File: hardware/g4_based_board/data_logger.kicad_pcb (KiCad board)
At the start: 4 copper layers, 290 parts, among them J1 Conn_01x07_Socket, J10 Screw_Terminal_01x03, J11 Screw_Terminal_01x03, J12 Conn_02x03_Odd_Even, J13 Conn_02x03_Odd_Even, J14 DE9_Receptacle, J15 Screw_Terminal_01x03, J16 Screw_Terminal_01x03, J17 Screw_Terminal_01x03, J18 Screw_Terminal_01x03, J19 Screw_Terminal_01x03, J2 Conn_02x07_Odd_Even, J20 Screw_Terminal_01x03, J21 Screw_Terminal_01x03, J22 Screw_Terminal_01x03, J23 Screw_Terminal_01x03, J24 Screw_Terminal_01x03, J25 Screw_Terminal_01x03, J26 Conn_02x03_Odd_Even, J27 Conn_02x03_Odd_Even, J28 DE9_Receptacle, J29 Screw_Terminal_01x03, J3 Conn_01x07_Socket, J30 Conn_02x03_Odd_Even, J31 Conn_02x03_Odd_Even, J32 DE9_Receptacle, J33 Conn_02x03_Odd_Even, J34 Conn_02x03_Odd_Even, J35 DE9_Receptacle, J36 Conn_02x03_Odd_Even, J37 Conn_02x03_Odd_Even, J38 DE9_Receptacle, J4 Conn_02x03_Odd_Even, J5 Conn_02x03_Odd_Even, J6 DE9_Receptacle, J7 Conn_01x05_Socket, J8 USB_C_Receptacle_USB2.0, J9 Micro_SD_Card_Det1, Q1 NPN, Q10 NMOS, Q11 NMOS, Q12 NMOS, Q13 NMOS, Q14 NMOS, Q15 NMOS, Q16 NMOS, Q17 NMOS, Q2 NPN, Q3 NMOS, Q4 NMOS, Q5 BC547, Q6 NMOS, Q7 NMOS, Q8 NMOS, Q9 NMOS, SW1 RESET, SW2 SW_SPDT, U1 STM32G431R6Tx, U2 MCP9804_MSOP, U3 MCP3428x-xST, U4 TXS0102DCT, U5 PCF8574, U6 tps2117, U7 AZ1117-3.3

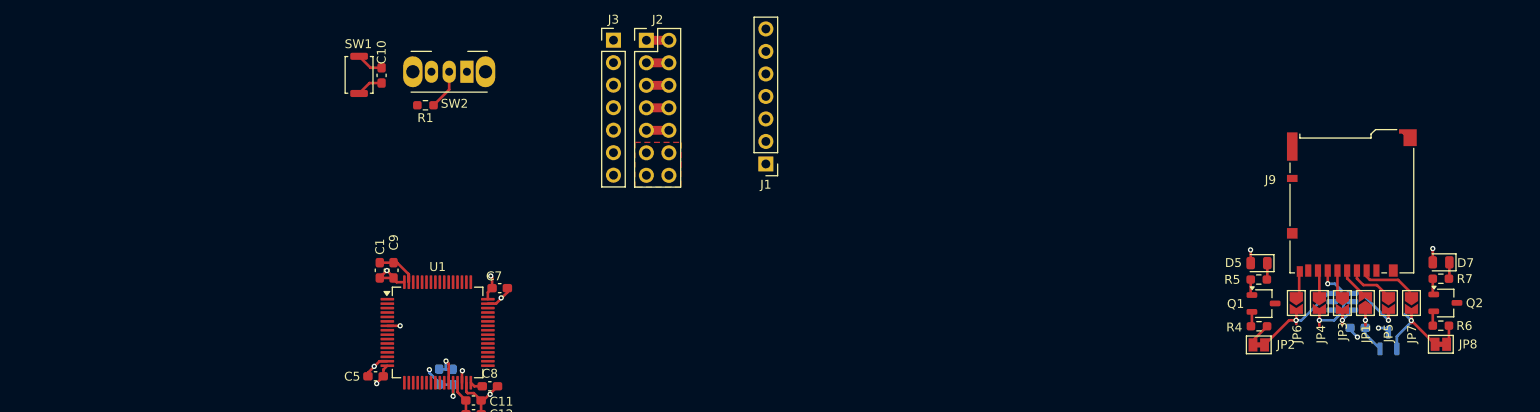
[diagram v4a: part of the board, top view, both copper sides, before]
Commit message: added buttons
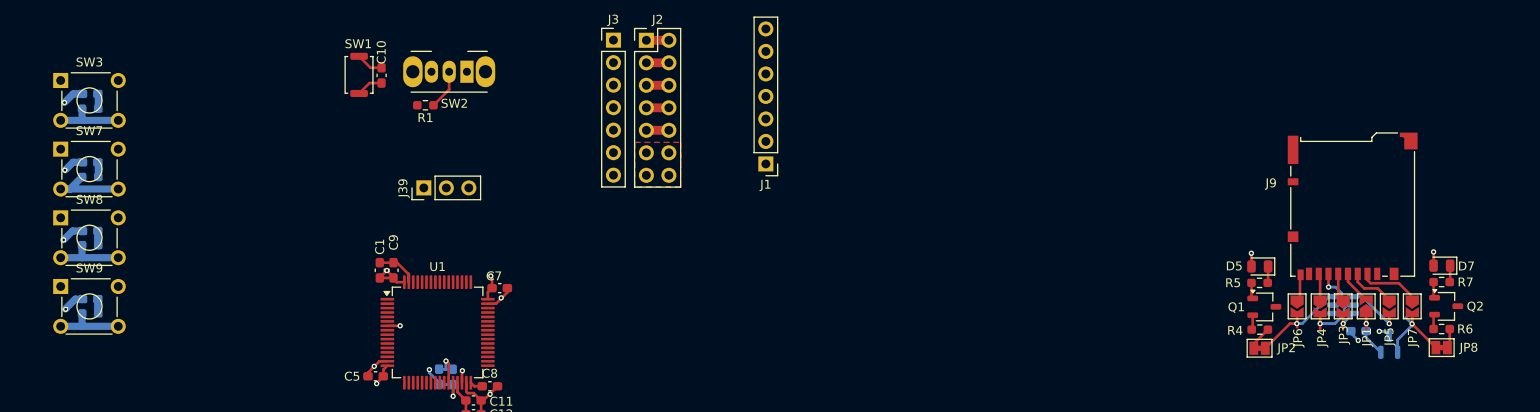
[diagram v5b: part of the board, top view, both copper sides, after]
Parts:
- added C53: C, Capacitor_SMD:C_0603_1608Metric_Pad1.08x0.95mm_HandSolder, B.Cu at (60.5, 26.6)
- added C54: C, Capacitor_SMD:C_0603_1608Metric_Pad1.08x0.95mm_HandSolder, B.Cu at (60.5, 34.3)
- added C55: C, Capacitor_SMD:C_0603_1608Metric_Pad1.08x0.95mm_HandSolder, B.Cu at (60.5, 42.1)
- added C56: C, Capacitor_SMD:C_0603_1608Metric_Pad1.08x0.95mm_HandSolder, B.Cu at (60.5, 49.8)
- added J39: Conn_01x03, Connector_PinHeader_2.54mm:PinHeader_1x03_P2.54mm_Vertical, F.Cu at (98.2, 37.2)
- added R73: R, Resistor_SMD:R_0603_1608Metric_Pad0.98x0.95mm_HandSolder, B.Cu at (60.5, 28.3)
- added R75: R, Resistor_SMD:R_0603_1608Metric_Pad0.98x0.95mm_HandSolder, B.Cu at (60.5, 36.0)
- added R77: R, Resistor_SMD:R_0603_1608Metric_Pad0.98x0.95mm_HandSolder, B.Cu at (60.5, 43.7)
- added R79: R, Resistor_SMD:R_0603_1608Metric_Pad0.98x0.95mm_HandSolder, B.Cu at (60.5, 51.4)
- added SW3: DOWN, Button_Switch_THT:SW_TH_Tactile_Omron_B3F-10xx, F.Cu at (57.2, 25.1)
- added SW7: DOWN, Button_Switch_THT:SW_TH_Tactile_Omron_B3F-10xx, F.Cu at (57.2, 32.9)
- added SW8: DOWN, Button_Switch_THT:SW_TH_Tactile_Omron_B3F-10xx, F.Cu at (57.2, 40.6)
- added SW9: DOWN, Button_Switch_THT:SW_TH_Tactile_Omron_B3F-10xx, F.Cu at (57.2, 48.4)
- moved D4 0.39 mm to (201.9, 50.4)
- moved R7 0.39 mm to (213.1, 47.9)
- moved JP2 0.39 mm to (192.5, 55.3)
- moved Q2 0.39 mm to (213.6, 50.6)
- moved R5 0.39 mm to (192.5, 47.9)
- moved C13 0.39 mm to (203.7, 53.4)
- moved D5 0.39 mm to (192.5, 46.1)
- moved D6 0.39 mm to (207.2, 54.8)
- moved D7 0.39 mm to (213.1, 46.0)
- moved J9 0.39 mm to (203.0, 39.3)
- moved JP1 0.39 mm to (204.6, 50.6)
- moved JP4 0.39 mm to (199.3, 50.6)
- moved JP5 0.39 mm to (207.2, 50.6)
- moved JP6 0.39 mm to (196.8, 50.6)
- moved JP7 0.39 mm to (209.8, 50.6)
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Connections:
- U1 pad 17: unconnected-(U1-PA3-Pad17) -> /analog_digital_io/GPIO-4
- U1 pad 22: /analog_digital_io/GPIO-11 -> /interface/SD_CONNECTED
- U1 pad 24: unconnected-(U1-PB0-Pad24) -> /analog_digital_io/GPIO-11
- U1 pad 26: unconnected-(U1-PB2-Pad26) -> /interface/WAKE_BTN
- U1 pad 30: unconnected-(U1-PB10-Pad30) -> /interface/ENTER_BTN
- U1 pad 33: unconnected-(U1-PB11-Pad33) -> /interface/DOWN_BTN
- U1 pad 34: /interface/SD_CONNECTED -> /analog_digital_io/GPIO-3
- U1 pad 35: /interface/SCLK -> /high_speed_digital/EN_1
- U1 pad 36: /interface/MISO -> /high_speed_digital/EN_2
- U1 pad 37: /interface/MOSI -> /high_speed_digital/EN_3
- U1 pad 42: /analog_digital_io/GPIO-3 -> unconnected-(U1-PA8-Pad42)
- U1 pad 50: /high_speed_digital/SDA -> /mcu/USART_TX
- U1 pad 51: /analog_digital_io/GPIO-4 -> /mcu/USART_RX
- U1 pad 52: /high_speed_digital/EN_1 -> /interface/SCLK
- U1 pad 53: /high_speed_digital/EN_2 -> /interface/MISO
- U1 pad 54: /high_speed_digital/EN_3 -> /interface/MOSI
- U1 pad 58: unconnected-(U1-PB5-Pad58) -> /mcu/USART_CK
- U1 pad 60: unconnected-(U1-PB7-Pad60) -> /high_speed_digital/SDA
- U1 pad 62: unconnected-(U1-PB9-Pad62) -> /interface/UP_BTN
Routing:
- net GND: track 812.8 -> 822.4 mm, vias 64 -> 68
- net Net-(R75-Pad1): track 0.00 -> 9.48 mm
- net Net-(R79-Pad1): track 0.00 -> 7.97 mm
- net Net-(R77-Pad1): track 0.00 -> 7.92 mm
- net Net-(R73-Pad1): track 0.00 -> 7.86 mm
- net /interface/ENTER_BTN: track 0.00 -> 3.01 mm, vias 0 -> 1
- net /interface/DOWN_BTN: track 0.00 -> 1.70 mm
- net /interface/UP_BTN: track 0.00 -> 1.68 mm
- net /interface/WAKE_BTN: track 0.00 -> 1.63 mm
- net unconnected-(U1-PB10-Pad30): track 1.39 -> 0.00 mm, vias 1 -> 0

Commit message: rev-1
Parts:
- removed C14, C15, C16, C17, C26, C27, C28, C29, C30, C31, C32, C33, C34, C35, C36, C37, C38, C39, C40, C41, C42, C43, C44, C45, C46, C47, C48, C49: C, Capacitor_SMD:C_0603_1608Metric_Pad1.08x0.95mm_HandSolder
- removed C23, C24, C25: 100n, Capacitor_SMD:C_0603_1608Metric_Pad1.08x0.95mm_HandSolder
- removed D10, D11, D12, D13, D14, D15, D16, D17, D18, D19, D20, D21, D8, D9: SP0502BAHT, Package_TO_SOT_SMD:SOT-23
- removed DS1: WC1602A, Display:WC1602A
- removed H2, H4, H5, H6, H7, H9: MountingHole, MountingHole:MountingHole_3.2mm_M3
- removed J10, J11, J15, J16, J17, J18, J19, J20, J21, J22, J23, J24, J25, J29: Screw_Terminal_01x03, TerminalBlock:TerminalBlock_Altech_AK300-3_P5.00mm
- removed J14, J28, J32, J35, J38, J6: DE9_Receptacle, Connector_Dsub:DSUB-9_Female_Vertical_P2.77x2.84mm_MountingHoles
- removed J26, J27, J30, J31, J33, J34, J36, J37: Conn_02x03_Odd_Even, Connector_PinHeader_2.54mm:PinHeader_2x03_P2.54mm_Vertical
- removed JP10, JP13, JP26, JP29, JP32, JP35, JP38, JP41, JP44, JP47, JP50, JP53, JP56, JP59: pulldown, Connector_PinHeader_2.54mm:PinHeader_1x02_P2.54mm_Vertical
- removed JP11, JP14, JP27, JP30, JP33, JP36, JP39, JP42, JP45, JP48, JP51, JP54, JP57, JP60: power_select, Connector_PinHeader_2.54mm:PinHeader_1x03_P2.54mm_Vertical
- removed JP12, JP25, JP28, JP31, JP34, JP37, JP40, JP43, JP46, JP49, JP52, JP55, JP58, JP9: I/O select, Connector_PinHeader_2.54mm:PinHeader_1x03_P2.54mm_Vertical
- removed JP20, JP21, JP22: SolderJumper_3_Open, Jumper:SolderJumper-3_P1.3mm_Open_RoundedPad1.0x1.5mm
- removed JP23, JP24, JP5, JP6, JP7: Jumper_2_Open, Jumper:SolderJumper-2_P1.3mm_Open_TrianglePad1.0x1.5mm
- removed Q10, Q11, Q12, Q13, Q14, Q15, Q16, Q17, Q3, Q4, Q6, Q7, Q8, Q9: NMOS, Package_TO_SOT_SMD:SOT-23-3
- removed R10, R11, R12, R13, R14, R15, R22, R23, R24, R25, R26, R27, R28, R29, R30, R31, R32, R33, R34, R35, R36, R37, R38, R39, R40, R41, R42, R43, R44, R45, R46, R47, R48, R49, R50, R51, R52, R53, R54, R55, R56, R57, R58, R59, R60, R61, R62, R63, R64, R65, R66, R67, R68, R69, R8, R9: R, Resistor_SMD:R_0603_1608Metric_Pad0.98x0.95mm_HandSolder
- removed TP5: LCD_PWR, TestPoint:TestPoint_Pad_D1.5mm
- removed U5: PCF8574, Package_SO:SOIC-16W_7.5x10.3mm_P1.27mm
- added G***: LOGO, frogs:UC_LOGO, B.Cu at (188.0, 136.0)
- added G***: LOGO, frogs:frog_smol, B.Cu at (167.0, 105.0)
- added J40: Conn_01x07_Socket, Connector_PinHeader_2.54mm:PinHeader_1x07_P2.54mm_Vertical, F.Cu at (106.8, 141.1)
- added J43: Conn_01x06, Connector_PinHeader_2.54mm:PinHeader_1x06_P2.54mm_Vertical, B.Cu at (165.2, 78.1)
- added R74: 1k, Resistor_SMD:R_0603_1608Metric_Pad0.98x0.95mm_HandSolder, B.Cu at (141.6, 90.6)
- added R76: 1k, Resistor_SMD:R_0603_1608Metric_Pad0.98x0.95mm_HandSolder, B.Cu at (126.1, 90.6)
- added R78: 1k, Resistor_SMD:R_0603_1608Metric_Pad0.98x0.95mm_HandSolder, B.Cu at (133.8, 90.6)
- added RV2: 10k, Potentiometer_THT:Potentiometer_Vishay_T73YP_Vertical, B.Cu at (142.6, 65.2)
- added RV3: 10k, Potentiometer_THT:Potentiometer_Vishay_T73YP_Vertical, B.Cu at (134.7, 65.2)
- added RV4: 10k, Potentiometer_THT:Potentiometer_Vishay_T73YP_Vertical, B.Cu at (142.5, 88.6)
- added RV5: 10k, Potentiometer_THT:Potentiometer_Vishay_T73YP_Vertical, B.Cu at (126.9, 65.2)
- added RV6: 10k, Potentiometer_THT:Potentiometer_Vishay_T73YP_Vertical, B.Cu at (119.1, 65.2)
- added RV7: 10k, Potentiometer_THT:Potentiometer_Vishay_T73YP_Vertical, B.Cu at (127.1, 88.6)
- added RV8: 10k, Potentiometer_THT:Potentiometer_Vishay_T73YP_Vertical, B.Cu at (134.7, 88.6)
- C1, C11, C12, C5, C7, C8, C9, J2, J7, J9, JP1, JP15, JP16, JP17, R1, SW2, TC1, TC2, TC3, TC4, U1: moved to B.Cu
- C18, C19, C2, C20, C6, D4, D6, JP18, JP19, R16, U2, U3: moved to F.Cu
- C21, C22: value 100n -> C; moved to F.Cu
- J12: value Conn_02x03_Odd_Even -> Screw_Terminal_01x04; footprint Connector_PinHeader_2.54mm:PinHeader_2x03_P2.54mm_Vertical -> TerminalBlock:TerminalBlock_Altech_AK300-4_P5.00mm; moved to B.Cu
- J13: value Conn_02x03_Odd_Even -> Conn_01x09_Pin; footprint Connector_PinHeader_2.54mm:PinHeader_2x03_P2.54mm_Vertical -> Connector_PinHeader_2.54mm:PinHeader_1x09_P2.54mm_Vertical; moved to B.Cu
- J4: value Conn_02x03_Odd_Even -> Conn_01x04; footprint Connector_PinHeader_2.54mm:PinHeader_2x03_P2.54mm_Vertical -> Connector_Molex:Molex_KK-254_AE-6410-04A_1x04_P2.54mm_Vertical
- J5: value Conn_02x03_Odd_Even -> Screw_Terminal_01x03; footprint Connector_PinHeader_2.54mm:PinHeader_2x03_P2.54mm_Vertical -> TerminalBlock:TerminalBlock_Altech_AK300-3_P5.00mm; moved to B.Cu
- JP3: value Jumper_2_Open -> power_select; footprint Jumper:SolderJumper-2_P1.3mm_Open_TrianglePad1.0x1.5mm -> Connector_PinHeader_2.54mm:PinHeader_1x03_P2.54mm_Vertical; moved to B.Cu
- JP4: value Jumper_2_Open -> Jumper_3_Bridged12; footprint Jumper:SolderJumper-2_P1.3mm_Open_TrianglePad1.0x1.5mm -> Connector_PinHeader_2.54mm:PinHeader_1x03_P2.54mm_Vertical; moved to B.Cu
- Q5: value BC547 -> NMOS
- R17, R18: value R -> 0; moved to F.Cu
- R19, R20: value 10k -> R
- R21: value 120 -> 1k
- RV1: footprint Potentiometer_THT:Potentiometer_Vishay_T73XX_Horizontal -> Potentiometer_THT:Potentiometer_Vishay_T73YP_Vertical
- SW7: value DOWN -> UP
- SW8: value DOWN -> ENTER
- SW9: value DOWN -> WAKE
- U4: value TXS0102DCT -> TL074; footprint Package_SO:SSOP-8_2.95x2.8mm_P0.65mm -> Package_SO:SOIC-14_3.9x8.7mm_P1.27mm
- moved H10 195.4 mm to (199.6, 146.8)
- moved H8 173.1 mm to (199.4, 54.2)
- moved R1 135.4 mm to (197.1, 120.6), turned to 90 degrees
- moved SW2 134.1 mm to (200.8, 115.9), turned to -90 degrees
- moved SW1 133.3 mm to (200.1, 100.9), turned to 180 degrees
- moved C10 130.7 mm to (197.6, 103.5), turned to 0 degrees
- moved C18 130.4 mm to (135.2, 145.7)
- moved R16 129.3 mm to (135.2, 144.2)
- moved TC3 129.2 mm to (149.5, 144.0)
- moved TC2 129.2 mm to (115.8, 144.0)
- moved TC4 129.2 mm to (138.3, 144.0)
- moved TC1 129.2 mm to (127.0, 144.0)
- moved R21 128.4 mm to (118.3, 90.7)
- moved R17 128.1 mm to (135.2, 142.6)
- moved J13 127.8 mm to (150.8, 77.7), turned to 180 degrees
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- renumbered TP31 to 3.3V, TP30 to 5v, TP32 to GND
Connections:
- C21 pad 1: /high_speed_digital/LCD1/LCD_Power_3.3 -> Net-(J5-Pin_1)
- C22 pad 1: /high_speed_digital/LCD1/LCD_Power -> Net-(JP4-C)
- D4 pad 3: /interface/SD_CONNECTED -> /interface/MOSI
- D4 pad 4: /interface/MOSI -> /interface/SCLK
- D4 pad 6: /interface/SCLK -> /interface/SD_CONNECTED
- D6 pad 1: /interface/SD_SELECT -> Net-(J5-Pin_1)
- D6 pad 2: +3.3V -> Net-(J5-Pin_2)
- J12 pad 1: +3.3V -> /analog_in/SIG_IN_1
- J12 pad 2: Net-(J12-Pin_2) -> /analog_in/SIG_IN_2
- J12 pad 3: +VDC -> /analog_in/SIG_IN_3
- J12 pad 4: Net-(J12-Pin_2) -> /analog_in/SIG_IN_4
- J13 pad 1: +BATT -> /mcu/ADC-GPIO-PWM-12
- J13 pad 2: Net-(J13-Pin_2) -> /mcu/DAC2_OUT-ADC-GPIO-PWM
- J13 pad 3: -VDC -> /mcu/DAC1_OUT-ADC-GPIO-PWM
- J13 pad 4: Net-(J13-Pin_2) -> /mcu/ADC-GPIO-PWM-4
- J13 pad 5: +5V -> /mcu/ADC-GPIO-PWM-2-DIFF1-2
- J13 pad 6: Net-(J13-Pin_2) -> /mcu/ADC-GPIO-PWM-1-DIFF1-1
- J2 pad 1: +5V -> +3.3V
- J2 pad 10: -VDC -> +BATT
- J2 pad 2: +5V -> +3.3V
- J2 pad 3: +3.3V -> +5V
- J2 pad 4: +3.3V -> +5V
- J2 pad 5: +BATT -> -VDC
- J2 pad 6: +BATT -> -VDC
- J2 pad 9: -VDC -> +BATT
- J39 pad 2: /mcu/USART_RX -> /mcu/USART_TX
- J39 pad 3: /mcu/USART_TX -> /mcu/USART_RX
- J4 pad 1: +3.3V -> /high_speed_digital/I2C_CLK
- J4 pad 2: Net-(J4-Pin_2) -> /high_speed_digital/SDA
- J4 pad 3: +VDC -> +3.3V
- J4 pad 4: Net-(J4-Pin_2) -> GND
- J5 pad 1: +BATT -> Net-(J5-Pin_1)
- J5 pad 3: -VDC -> GND
- J7 pad 3: /high_speed_digital/SCLK -> /high_speed_digital/MISO
- J7 pad 5: /high_speed_digital/MISO -> /high_speed_digital/SCLK
- JP3 pad 1: /interface/SCLK -> +5V
- JP3 pad 2: /interface/SCLK -> Net-(J5-Pin_1)
- JP4 pad 1: /interface/MISO -> +5V
- JP4 pad 2: /interface/MISO -> Net-(JP4-C)
- Q5 pad 1: Net-(DS1-LED(-)) -> Net-(J5-Pin_2)
- Q5 pad 2: Net-(Q5-B) -> Net-(Q5-G)
- Q5 pad 3: GND -> Net-(Q5-S)
- R19 pad 1: Net-(U4-OE) -> Net-(Q5-G)
- R19 pad 2: GND -> /mcu/ADC-GPIO-PWM-11
- R20 pad 1: Net-(Q5-B) -> Net-(Q5-S)
- R20 pad 2: /high_speed_digital/LCD1/led -> GND
- R21 pad 1: /high_speed_digital/LCD1/LCD_Power -> GND
- R21 pad 2: Net-(DS1-LED(+)) -> Net-(U4B--)
- RV1 pad 1: GND -> Net-(U4B--)
- RV1 pad 2: Net-(DS1-VO) -> /mcu/HSE_IN
- RV1 pad 3: /high_speed_digital/LCD1/LCD_Power -> GND
- U1 pad 10: /analog_digital_io/GPIO-9 -> /mcu/ADC-GPIO-PWM-9
- U1 pad 11: /analog_digital_io/GPIO-10 -> /mcu/ADC-GPIO-PWM-10
- U1 pad 12: /analog_digital_io/GPIO-1 -> /mcu/ADC-GPIO-PWM-1-DIFF1-1
- U1 pad 13: /analog_digital_io/GPIO-2 -> /mcu/ADC-GPIO-PWM-2-DIFF1-2
- U1 pad 14: unconnected-(U1-PA2-Pad14) -> /interface/WAKE_BTN
- U1 pad 17: /analog_digital_io/GPIO-4 -> /mcu/ADC-GPIO-PWM-4
- U1 pad 18: /analog_digital_io/GPIO-2-DAC -> /mcu/DAC1_OUT-ADC-GPIO-PWM
- U1 pad 19: /analog_digital_io/GPIO-1-DAC -> /mcu/DAC2_OUT-ADC-GPIO-PWM
- U1 pad 2: /high_speed_digital/EN_4 -> /interface/DOWN_BTN
- U1 pad 22: /interface/SD_CONNECTED -> unconnected-(U1-PC4-Pad22)
- U1 pad 23: /analog_digital_io/GPIO-12 -> /mcu/ADC-GPIO-PWM-12
- U1 pad 24: /analog_digital_io/GPIO-11 -> /mcu/ADC-GPIO-PWM-11
- U1 pad 25: unconnected-(U1-PB1-Pad25) -> /mcu/DIGITAL_IO_EN_4
- U1 pad 26: /interface/WAKE_BTN -> /mcu/PWR_STATUS
- U1 pad 3: /high_speed_digital/EN_5 -> /interface/UP_BTN
- U1 pad 30: /interface/ENTER_BTN -> /mcu/DIGITAL_IO_EN_5
- U1 pad 33: /interface/DOWN_BTN -> /mcu/DIGITAL_IO_EN_6
- U1 pad 34: /analog_digital_io/GPIO-3 -> /mcu/ADC-GPIO-PWM-3
- U1 pad 35: /high_speed_digital/EN_1 -> /mcu/DIGITAL_IO_EN_1
- U1 pad 36: /high_speed_digital/EN_2 -> /mcu/DIGITAL_IO_EN_2
- U1 pad 37: /high_speed_digital/EN_3 -> /mcu/DIGITAL_IO_EN_3
- U1 pad 38: /interface/SD_SELECT -> /mcu/COMMS_EN_1
- U1 pad 39: /mcu/COMMS_EN_1 -> /mcu/COMMS_EN_2
- U1 pad 4: /high_speed_digital/EN_6 -> /interface/ENTER_BTN
- U1 pad 40: /mcu/COMMS_EN_2 -> /mcu/COMMS_EN_3
- U1 pad 41: /mcu/COMMS_EN_3 -> /interface/SD_SELECT
- U1 pad 55: /mcu/PWR_STATUS -> unconnected-(U1-PD2-Pad55)
- U1 pad 62: /interface/UP_BTN -> /interface/SD_CONNECTED
- U1 pad 8: /analog_digital_io/GPIO-7 -> /analog_in/ADC_4
- U1 pad 9: /analog_digital_io/GPIO-8 -> /analog_in/ADC_2
- U4 pad 1: /high_speed_digital/LCD1/5v_SDA -> /analog_in/ADC_2
- U4 pad 2: GND -> Net-(U4A--)
- U4 pad 3: /high_speed_digital/LCD1/LCD_Power_3.3 -> Net-(U4A-+)
- U4 pad 4: /high_speed_digital/SDA -> Net-(JP4-C)
- U4 pad 5: /high_speed_digital/I2C_CLK -> Net-(U4B-+)
- U4 pad 6: Net-(U4-OE) -> Net-(U4B--)
- U4 pad 7: /high_speed_digital/LCD1/LCD_Power -> /mcu/HSE_IN
- U4 pad 8: /high_speed_digital/LCD1/5v_SCL -> /mcu/HSE_OUT
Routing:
- net GND: track 822.4 -> 108.1 mm, vias 68 -> 46
- net +5V: track 32.8 -> 212.1 mm, vias 4 -> 2
- net -VDC: track 2.54 -> 170.1 mm, vias 0 -> 2
- net +BATT: track 2.54 -> 168.9 mm, vias 0 -> 2
- net +VDC: track 2.54 -> 166.6 mm, vias 0 -> 2
- net +3.3V: track 50.7 -> 177.1 mm, vias 16 -> 17
- net Net-(J21-Pin_2): track 103.2 -> 0.00 mm, vias 3 -> 0
- net Net-(J22-Pin_2): track 103.2 -> 0.00 mm, vias 3 -> 0
- net Net-(J16-Pin_2): track 103.2 -> 0.00 mm, vias 3 -> 0
- net Net-(J10-Pin_2): track 103.2 -> 0.00 mm, vias 3 -> 0
- net Net-(J23-Pin_2): track 103.2 -> 0.00 mm, vias 3 -> 0
- net Net-(J24-Pin_2): track 103.2 -> 0.00 mm, vias 3 -> 0
- net Net-(J20-Pin_2): track 103.2 -> 0.00 mm, vias 3 -> 0
- net Net-(J18-Pin_2): track 103.2 -> 0.00 mm, vias 3 -> 0
- net Net-(J15-Pin_2): track 103.2 -> 0.00 mm, vias 3 -> 0
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- added copper zone on In1.Cu, net +3.3V
- added copper zone on B.Cu, net GND
- added copper zone on In2.Cu, net GND
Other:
- board outline added: 100 x 100 mm
- board text added: "+VDC"
- board text added: "+dB"
- board text added: "-VDC"
- board text added: "-dB"
- board text added: "3.3V"
- board text added: "3.3v"
- board text added: "5V"
- board text added: "5_Pv"
- board text added: "5v"
- board text added: "5v 4A MAX"
- board text added: "ADC-10"
- board text added: "ADC-12"
- board text added: "ADC-1_DIFF_1"
- board text added: "ADC-2_DIFF_2"
- board text added: "ADC-3"
- board text added: "ADC-4"
- board text added: "ADC-9"
- board text added: "BAT_MONITOR"
- board text added: "BOOT_MODE"
- board text added: "CLK"
- board text added: "COMMS_MODULE"
- board text added: "COMM_EN_1"
- board text added: "COMM_EN_2"
- board text added: "COMM_EN_3"
- board text added: "DAC1"
- board text added: "DAC2"
- board text added: "DOWN"
- board text added: "EN-1"
- board text added: "EN-2"
- board text added: "EN-3"
- board text added: "EN-4"
- board text added: "EN-5"
- board text added: "EN-6"
- board text added: "ENEL-400W-GROUP-E31"
- board text added: "ENTER"
- board text added: "FLASH"
- board text added: "GIPO w/ ADC"
- board text added: "GND"
- board text added: "ID: 72740637"
- board text added: "INPUT_GAIN"
- board text added: "LOGAN HENDERSON"
- board text added: "MISO"
- board text added: "MOSI"
- board text added: "OUTPUT_GAIN"
- board text added: "POWER_MODULE"
- board text added: "POWER_SELC"
- board text added: "PWM-GND"
- board text added: "PWR"
- board text added: "RESET"
- board text added: "SCLK"
- board text added: "SD CARD"
- board text added: "SDA"
- board text added: "SD_CONNECTED"
- board text added: "SD_SELECT"
- board text added: "SIG_1"
- board text added: "SIG_1_IN"
- board text added: "SIG_2"
- board text added: "SIG_2_IN"
- board text added: "SIG_3"
- board text added: "SIG_3_IN"
- board text added: "SIG_4"
- board text added: "SIG_4_IN"
- board text added: "STM32G431RBT6"
- board text added: "TC1"
- board text added: "TC2"
- board text added: "TC3"
- board text added: "TC4"
- board text added: "UP"
- board text added: "USART_CLK"
- board text added: "USART_RX"
- board text added: "USART_TX"
- board text added: "USB"
- board text added: "VBAT"
- board text added: "WAKE"
- board text added: "digital_EN"
- board text added: "https://eng-git.canterbury.ac.nz/lhe68/enel400-data-logger"
- board text added: "if you dont need to re program it select boot mode to flash connect to power"
- board text added: "supports USB PD"
- board text added: "to start programming make sure boot mode is on usb open stm32cubeIDE windows will make the connect noise open up main and start programmming click run to build and upload the code"
- board text added: "universal data logger"
- board text added: "yes is know the routing is bad, no time"

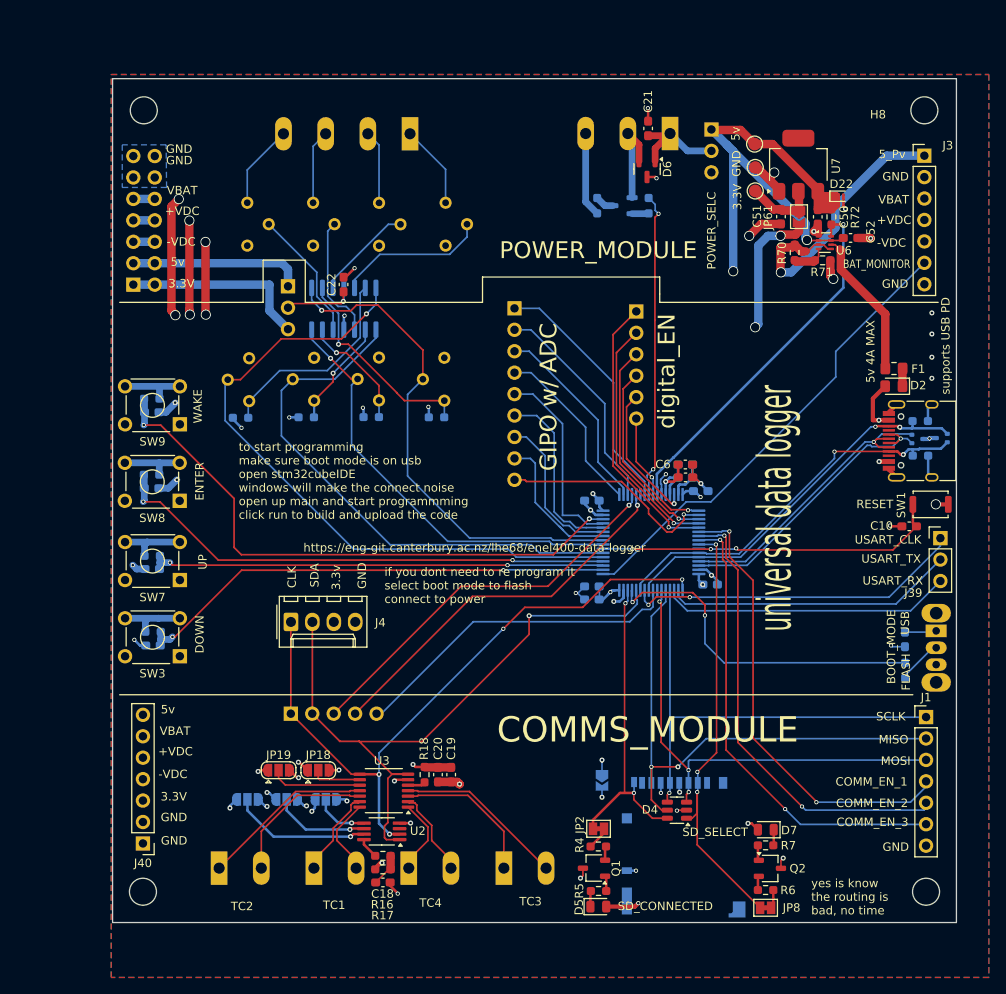
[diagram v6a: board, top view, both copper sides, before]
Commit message: updated .ioc to reflect changes make in pcb
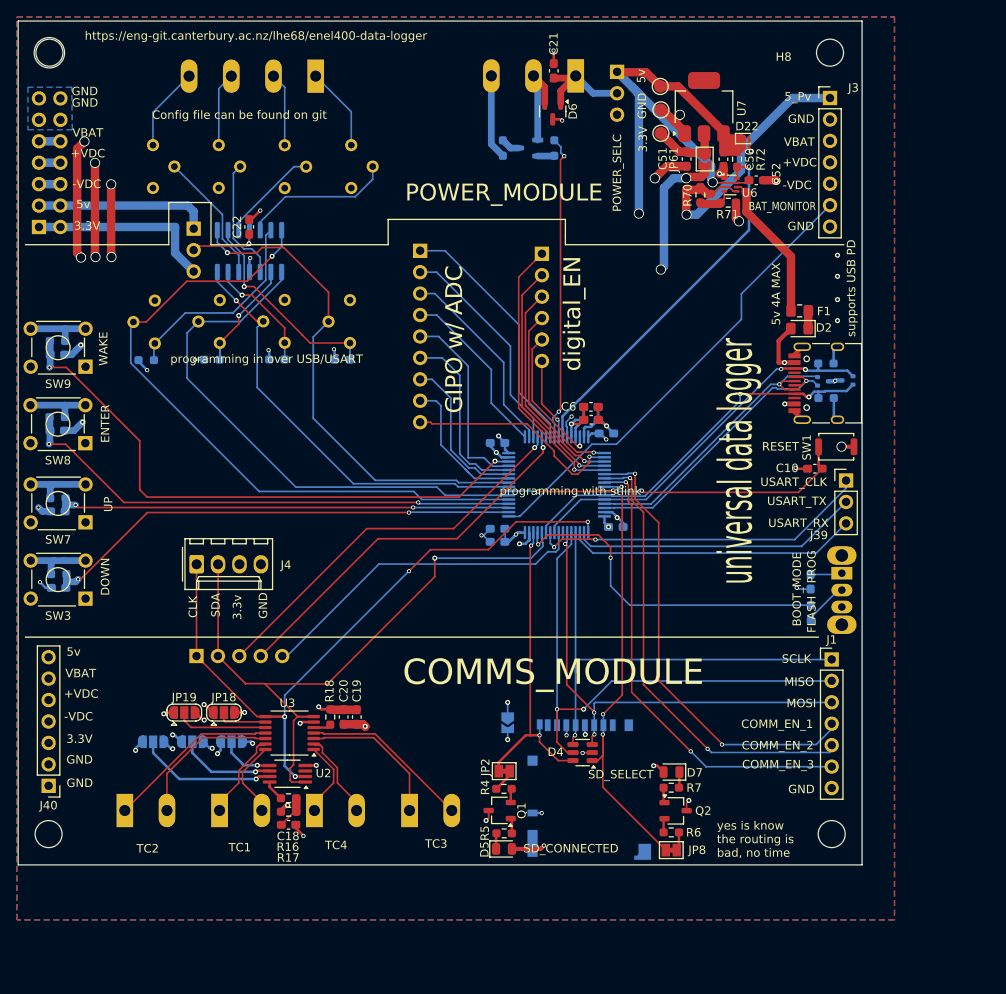
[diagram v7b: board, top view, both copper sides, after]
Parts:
- moved C2 13.1 mm to (159.9, 90.9)
- moved C5 13.1 mm to (148.8, 93.7)
- moved C8 13.1 mm to (161.7, 92.5)
- moved G*** 13.1 mm to (176.8, 129.2)
- moved H1 13.1 mm to (95.6, 140.0)
- moved H10 13.1 mm to (188.4, 140.0)
- moved J40 13.1 mm to (95.6, 134.3)
- moved J7 13.1 mm to (113.1, 118.9)
- moved JP1 13.1 mm to (150.0, 126.8)
- moved JP15 13.1 mm to (108.0, 129.1)
- moved JP17 13.1 mm to (117.3, 129.1)
- moved JP8 13.1 mm to (169.4, 141.9)
- moved Q1 13.1 mm to (149.0, 137.2)
- moved R6 13.1 mm to (169.4, 139.8)
- moved R7 13.1 mm to (169.4, 134.5)
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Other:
- outline, holes or cut-outs redrawn
- board text added: "Config file can be found on git"
- board text added: "PROG"
- board text added: "programming in over USB/USART"
- board text added: "programming with stlink"
- board text removed: "USB"
- board text removed: "if you dont need to re program it select boot mode to flash connect to power"
- board text removed: "to start programming make sure boot mode is on usb open stm32cubeIDE windows will make the connect noise open up main and start programmming click run to build and upload the code"
